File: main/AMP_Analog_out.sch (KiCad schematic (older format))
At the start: 12 parts, among them U6 TPA6110A2DGN

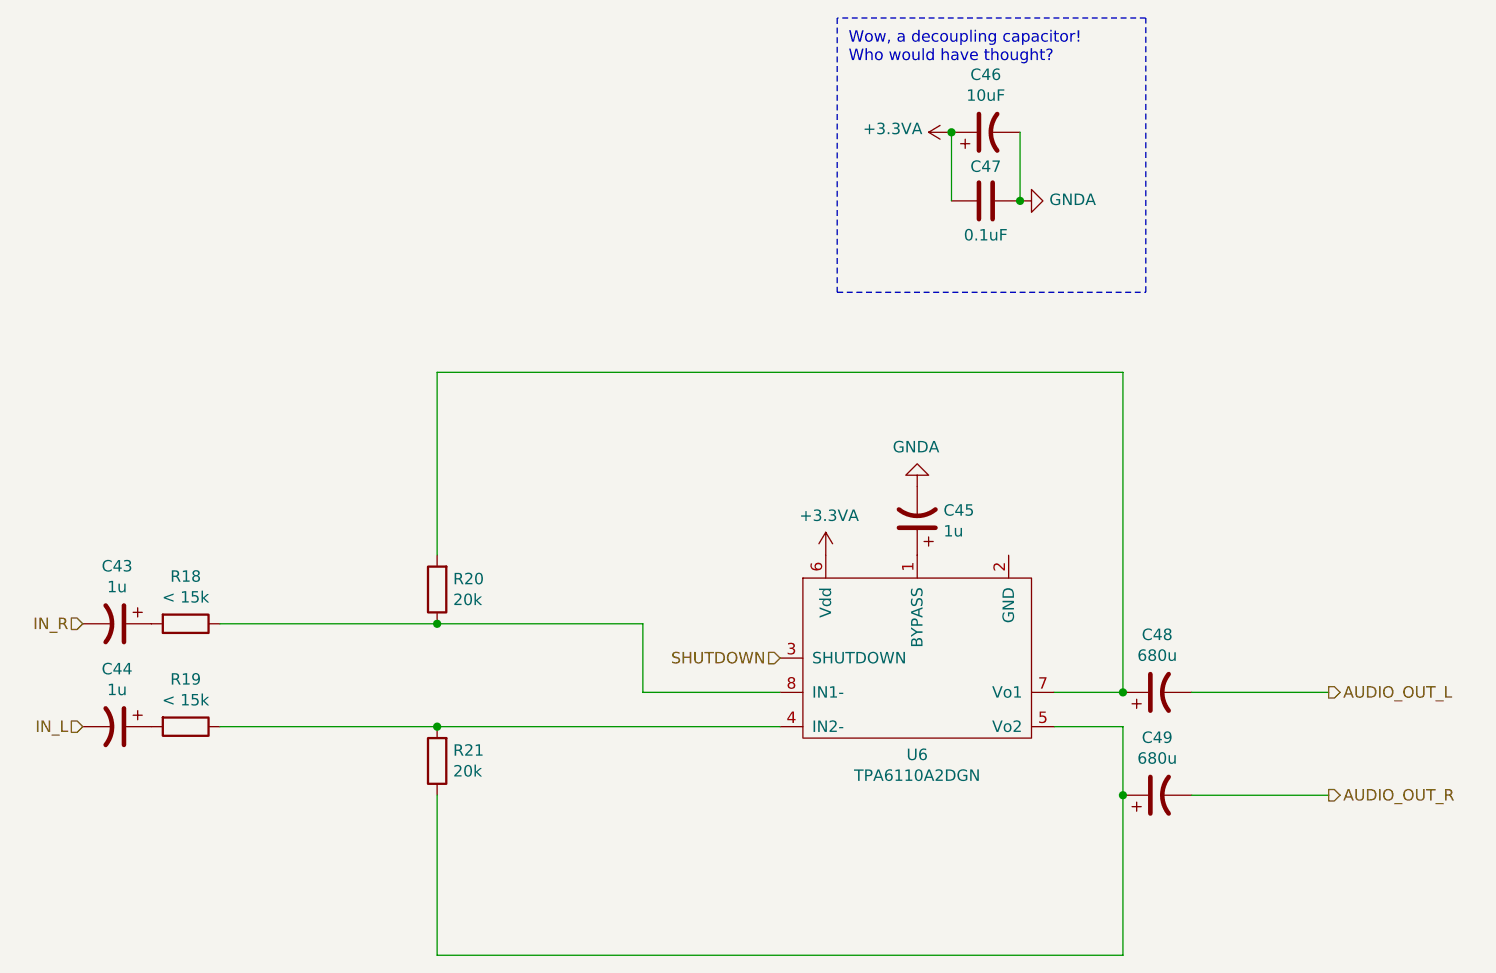
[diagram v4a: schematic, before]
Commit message: Be consistent with capacitor values (always use F)
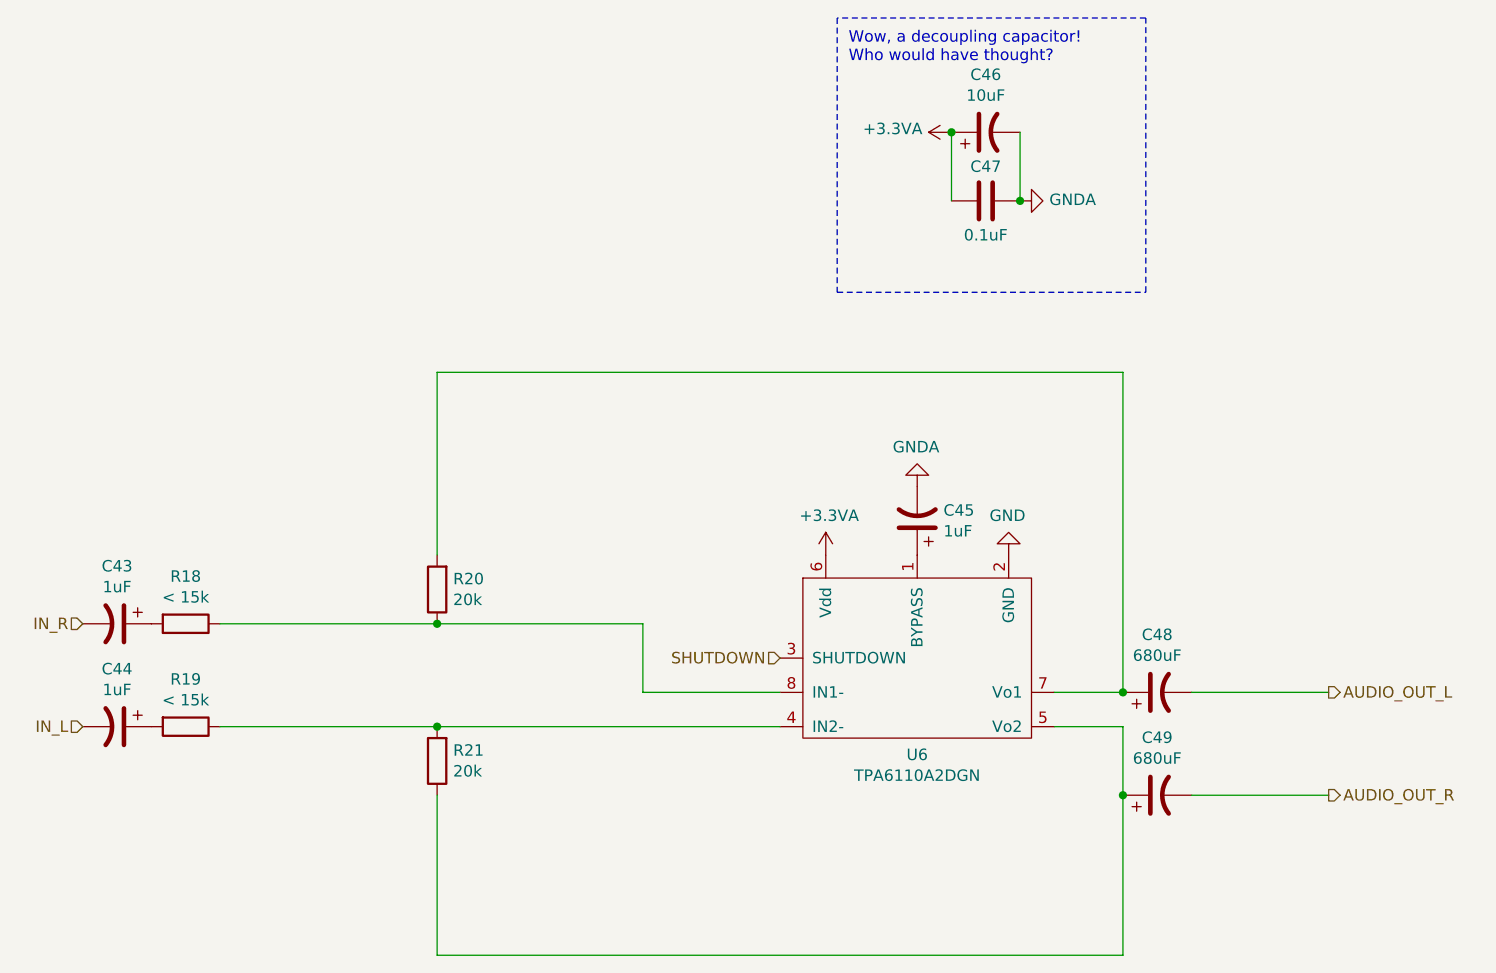
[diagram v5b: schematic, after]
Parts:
- C43, C44, C45: value 1u -> 1uF
- C48, C49: value 680u -> 680uF
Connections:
- net GND: now reaches U6.2 (GND)
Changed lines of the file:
@@
 $Descr A4 11693 8268
 encoding utf-8
-Sheet 6 7
+Sheet 5 7
 Title ""
 Date ""
@@
 P 6000 3250
 F 0 "C45" H 5885 3204 50  0000 R CNN
-F 1 "1u" H 5885 3295 50  0000 R CNN
+F 1 "1uF" H 5885 3295 50  0000 R CNN
 F 2 "" H 6000 3250 50  0001 C CNN
 F 3 "~" H 6000 3250 50  0001 C CNN
@@
 P 2500 3700
 F 0 "C43" V 2248 3700 50  0000 C CNN
-F 1 "1u" V 2339 3700 50  0000 C CNN
+F 1 "1uF" V 2339 3700 50  0000 C CNN
 F 2 "" H 2500 3700 50  0001 C CNN
 F 3 "~" H 2500 3700 50  0001 C CNN
@@
 P 2500 4150
 F 0 "C44" V 2248 4150 50  0000 C CNN
-F 1 "1u" V 2339 4150 50  0000 C CNN
+F 1 "1uF" V 2339 4150 50  0000 C CNN
 F 2 "" H 2500 4150 50  0001 C CNN
 F 3 "~" H 2500 4150 50  0001 C CNN
@@
 P 7050 4000
 F 0 "C48" V 7302 4000 50  0000 C CNN
-F 1 "680u" V 7211 4000 50  0000 C CNN
+F 1 "680uF" V 7211 4000 50  0000 C CNN
 F 2 "" H 7050 4000 50  0001 C CNN
 F 3 "~" H 7050 4000 50  0001 C CNN
@@
 P 7050 4450
 F 0 "C49" V 7302 4450 50  0000 C CNN
-F 1 "680u" V 7211 4450 50  0000 C CNN
+F 1 "680uF" V 7211 4450 50  0000 C CNN
 F 2 "" H 7050 4450 50  0001 C CNN
 F 3 "~" H 7050 4450 50  0001 C CNN
@@
 Text HLabel 7800 4450 2    50   Output ~ 0
 AUDIO_OUT_R
+$Comp
+L power:GND #PWR0166
+U 1 1 614CAB2C
+P 6400 3400
+F 0 "#PWR0166" H 6400 3150 50  0001 C CNN
+F 1 "GND" H 6405 3227 50  0000 C CNN
+F 2 "" H 6400 3400 50  0001 C CNN
+F 3 "" H 6400 3400 50  0001 C CNN
+	1    6400 3400
+	-1   0    0    1
+$EndComp
 $EndSCHEMATC

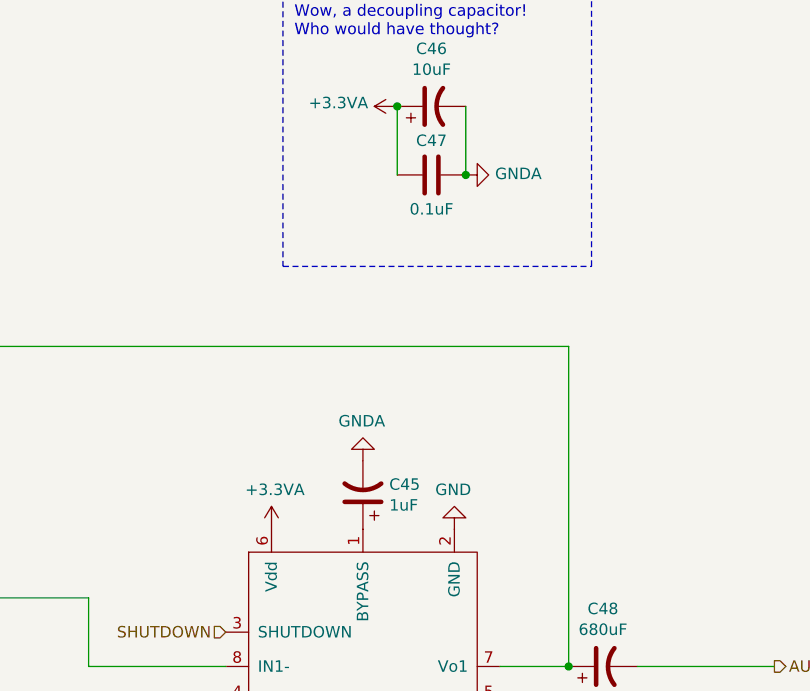
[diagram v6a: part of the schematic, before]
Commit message: Add FPGA RAM chip
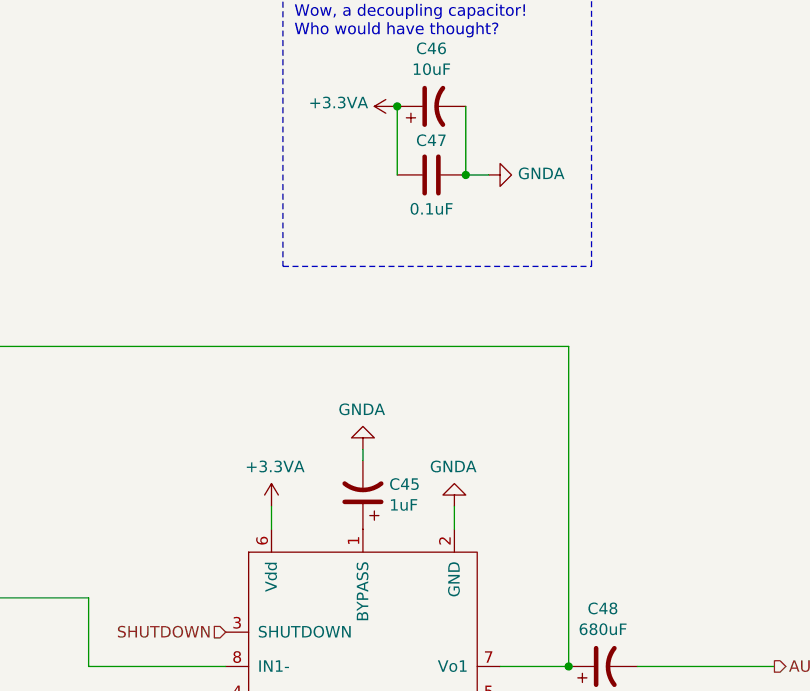
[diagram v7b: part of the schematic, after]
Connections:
- net GND is gone; now on net GNDA: U6.2 (GND)
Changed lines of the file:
@@
 $Descr A4 11693 8268
 encoding utf-8
-Sheet 5 7
+Sheet 3 7
 Title "MIDI Audio Box"
 Date "2021-09-21"
@@
 L power:+3.3VA #PWR0154
 U 1 1 6144EAAF
-P 5600 3400
-F 0 "#PWR0154" H 5600 3250 50  0001 C CNN
-F 1 "+3.3VA" H 5615 3573 50  0000 C CNN
-F 2 "" H 5600 3400 50  0001 C CNN
-F 3 "" H 5600 3400 50  0001 C CNN
-	1    5600 3400
+P 5600 3300
+F 0 "#PWR0154" H 5600 3150 50  0001 C CNN
+F 1 "+3.3VA" H 5615 3473 50  0000 C CNN
+F 2 "" H 5600 3300 50  0001 C CNN
+F 3 "" H 5600 3300 50  0001 C CNN
+	1    5600 3300
 	1    0    0    -1
 $EndComp
@@
 L power:GNDA #PWR0155
 U 1 1 6144FB76
-P 6450 1850
-F 0 "#PWR0155" H 6450 1600 50  0001 C CNN
-F 1 "GNDA" V 6455 1722 50  0000 R CNN
-F 2 "" H 6450 1850 50  0001 C CNN
-F 3 "" H 6450 1850 50  0001 C CNN
-	1    6450 1850
+P 6550 1850
+F 0 "#PWR0155" H 6550 1600 50  0001 C CNN
+F 1 "GNDA" V 6555 1722 50  0000 R CNN
+F 2 "" H 6550 1850 50  0001 C CNN
+F 3 "" H 6550 1850 50  0001 C CNN
+	1    6550 1850
 	0    -1   -1   0
 $EndComp
@@
 L power:GNDA #PWR0156
 U 1 1 61450313
-P 6000 3100
-F 0 "#PWR0156" H 6000 2850 50  0001 C CNN
-F 1 "GNDA" H 6005 2927 50  0000 C CNN
-F 2 "" H 6000 3100 50  0001 C CNN
-F 3 "" H 6000 3100 50  0001 C CNN
-	1    6000 3100
+P 6000 3050
+F 0 "#PWR0156" H 6000 2800 50  0001 C CNN
+F 1 "GNDA" H 6005 2877 50  0000 C CNN
+F 2 "" H 6000 3050 50  0001 C CNN
+F 3 "" H 6000 3050 50  0001 C CNN
+	1    6000 3050
 	-1   0    0    1
 $EndComp
@@
 Text HLabel 7800 4450 2    50   Output ~ 0
 AUDIO_OUT_R
-$Comp
-L power:GND #PWR0166
-U 1 1 614CAB2C
-P 6400 3400
-F 0 "#PWR0166" H 6400 3150 50  0001 C CNN
-F 1 "GND" H 6405 3227 50  0000 C CNN
-F 2 "" H 6400 3400 50  0001 C CNN
-F 3 "" H 6400 3400 50  0001 C CNN
-	1    6400 3400
-	-1   0    0    1
-$EndComp
+Wire Wire Line
+	6550 1850 6450 1850
+Wire Wire Line
+	6000 3100 6000 3050
+Wire Wire Line
+	5600 3300 5600 3400
+Wire Wire Line
+	6400 3300 6400 3400
+$Comp
+L power:GNDA #PWR0152
+U 1 1 616EC208
+P 6400 3300
+F 0 "#PWR0152" H 6400 3050 50  0001 C CNN
+F 1 "GNDA" H 6405 3127 50  0000 C CNN
+F 2 "" H 6400 3300 50  0001 C CNN
+F 3 "" H 6400 3300 50  0001 C CNN
+	1    6400 3300
+	-1   0    0    1
+$EndComp

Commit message: Final cleanup before sending in for rebiew
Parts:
- renumbered C43 to C1, C44 to C2, C45 to C3, C46 to C4, C47 to C5, C48 to C6, C49 to C7, R20 to R10, R21 to R11, R18 to R8, R19 to R9, U6 to U2
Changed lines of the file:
@@
 $EndDescr
 $Comp
-L TPA6110A2DGN:TPA6110A2DGN U6
+L TPA6110A2DGN:TPA6110A2DGN U2
 U 1 1 614497DA
 P 6000 3850
-F 0 "U6" H 6000 3427 50  0000 C CNN
+F 0 "U2" H 6000 3427 50  0000 C CNN
 F 1 "TPA6110A2DGN" H 6000 3336 50  0000 C CNN
 F 2 "" H 5650 3750 50  0001 C CNN
@@
 SHUTDOWN
 $Comp
-L power:+3.3VA #PWR0154
+L power:+3.3VA #PWR07
 U 1 1 6144EAAF
 P 5600 3300
-F 0 "#PWR0154" H 5600 3150 50  0001 C CNN
+F 0 "#PWR07" H 5600 3150 50  0001 C CNN
 F 1 "+3.3VA" H 5615 3473 50  0000 C CNN
 F 2 "" H 5600 3300 50  0001 C CNN
@@
 $EndComp
 $Comp
-L power:GNDA #PWR0155
+L power:GNDA #PWR011
 U 1 1 6144FB76
 P 6550 1850
-F 0 "#PWR0155" H 6550 1600 50  0001 C CNN
+F 0 "#PWR011" H 6550 1600 50  0001 C CNN
 F 1 "GNDA" V 6555 1722 50  0000 R CNN
 F 2 "" H 6550 1850 50  0001 C CNN
@@
 $EndComp
 $Comp
-L power:GNDA #PWR0156
+L power:GNDA #PWR08
 U 1 1 61450313
 P 6000 3050
-F 0 "#PWR0156" H 6000 2800 50  0001 C CNN
+F 0 "#PWR08" H 6000 2800 50  0001 C CNN
 F 1 "GNDA" H 6005 2877 50  0000 C CNN
 F 2 "" H 6000 3050 50  0001 C CNN
@@
 $EndComp
 $Comp
-L Device:CP1 C45
+L Device:CP1 C3
 U 1 1 61450A21
 P 6000 3250
-F 0 "C45" H 5885 3204 50  0000 R CNN
+F 0 "C3" H 5885 3204 50  0000 R CNN
 F 1 "1uF" H 5885 3295 50  0000 R CNN
 F 2 "" H 6000 3250 50  0001 C CNN
@@
 $EndComp
 $Comp
-L power:+3.3VA #PWR0157
+L power:+3.3VA #PWR09
 U 1 1 614535B7
 P 6150 1550
-F 0 "#PWR0157" H 6150 1400 50  0001 C CNN
+F 0 "#PWR09" H 6150 1400 50  0001 C CNN
 F 1 "+3.3VA" V 6165 1677 50  0000 L CNN
 F 2 "" H 6150 1550 50  0001 C CNN
@@
 $EndComp
 $Comp
-L Device:CP1 C46
+L Device:CP1 C4
 U 1 1 61453C17
 P 6300 1550
-F 0 "C46" V 6552 1550 50  0000 C CNN
+F 0 "C4" V 6552 1550 50  0000 C CNN
 F 1 "10uF" V 6461 1550 50  0000 C CNN
 F 2 "" H 6300 1550 50  0001 C CNN
@@
 	7000 1050 5650 1050
 $Comp
-L Device:CP1 C43
+L Device:CP1 C1
 U 1 1 61459645
 P 2500 3700
-F 0 "C43" V 2248 3700 50  0000 C CNN
+F 0 "C1" V 2248 3700 50  0000 C CNN
 F 1 "1uF" V 2339 3700 50  0000 C CNN
 F 2 "" H 2500 3700 50  0001 C CNN
@@
 $EndComp
 $Comp
-L Device:CP1 C44
+L Device:CP1 C2
 U 1 1 6145AB50
 P 2500 4150
-F 0 "C44" V 2248 4150 50  0000 C CNN
+F 0 "C2" V 2248 4150 50  0000 C CNN
 F 1 "1uF" V 2339 4150 50  0000 C CNN
 F 2 "" H 2500 4150 50  0001 C CNN
@@
 $EndComp
 $Comp
-L Device:R R18
+L Device:R R8
 U 1 1 6145F753
 P 2800 3700
-F 0 "R18" V 2593 3700 50  0000 C CNN
+F 0 "R8" V 2593 3700 50  0000 C CNN
 F 1 "< 15k" V 2684 3700 50  0000 C CNN
 F 2 "" V 2730 3700 50  0001 C CNN
@@
 $EndComp
 $Comp
-L Device:R R19
+L Device:R R9
 U 1 1 614603F8
 P 2800 4150
-F 0 "R19" V 2593 4150 50  0000 C CNN
+F 0 "R9" V 2593 4150 50  0000 C CNN
 F 1 "< 15k" V 2684 4150 50  0000 C CNN
 F 2 "" V 2730 4150 50  0001 C CNN
@@
 	2950 4150 3900 4150
 $Comp
-L Device:R R20
+L Device:R R10
 U 1 1 6146A9F3
 P 3900 3550
-F 0 "R20" H 3830 3504 50  0000 R CNN
+F 0 "R10" H 3830 3504 50  0000 R CNN
 F 1 "20k" H 3830 3595 50  0000 R CNN
 F 2 "" V 3830 3550 50  0001 C CNN
@@
 	3900 3700 4800 3700
 $Comp
-L Device:R R21
+L Device:R R11
 U 1 1 6146B124
 P 3900 4300
-F 0 "R21" H 3830 4254 50  0000 R CNN
+F 0 "R11" H 3830 4254 50  0000 R CNN
 F 1 "20k" H 3830 4345 50  0000 R CNN
 F 2 "" V 3830 4300 50  0001 C CNN
@@
 	3900 5150 3900 4450
 $Comp
-L Device:CP1 C48
+L Device:CP1 C6
 U 1 1 6146CB5D
 P 7050 4000
-F 0 "C48" V 7302 4000 50  0000 C CNN
+F 0 "C6" V 7302 4000 50  0000 C CNN
 F 1 "680uF" V 7211 4000 50  0000 C CNN
 F 2 "" H 7050 4000 50  0001 C CNN
@@
 Connection ~ 6900 4000
 $Comp
-L Device:CP1 C49
+L Device:CP1 C7
 U 1 1 6146D43E
 P 7050 4450
-F 0 "C49" V 7302 4450 50  0000 C CNN
+F 0 "C7" V 7302 4450 50  0000 C CNN
 F 1 "680uF" V 7211 4450 50  0000 C CNN
 F 2 "" H 7050 4450 50  0001 C CNN
@@
 	6900 4450 6900 5150
 $Comp
-L Device:C C47
+L Device:C C5
 U 1 1 6146271B
 P 6300 1850
-F 0 "C47" V 6150 1850 50  0000 C CNN
+F 0 "C5" V 6150 1850 50  0000 C CNN
 F 1 "0.1uF" V 6450 1850 50  0000 C CNN
 F 2 "" H 6338 1700 50  0001 C CNN
@@
 	6400 3300 6400 3400
 $Comp
-L power:GNDA #PWR0152
+L power:GNDA #PWR010
 U 1 1 616EC208
 P 6400 3300
-F 0 "#PWR0152" H 6400 3050 50  0001 C CNN
+F 0 "#PWR010" H 6400 3050 50  0001 C CNN
 F 1 "GNDA" H 6405 3127 50  0000 C CNN
 F 2 "" H 6400 3300 50  0001 C CNN
